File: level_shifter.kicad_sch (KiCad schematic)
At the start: 13 parts, among them U11 74LVC8T245, U12 74AVC4T245, U13 74LVC8T245

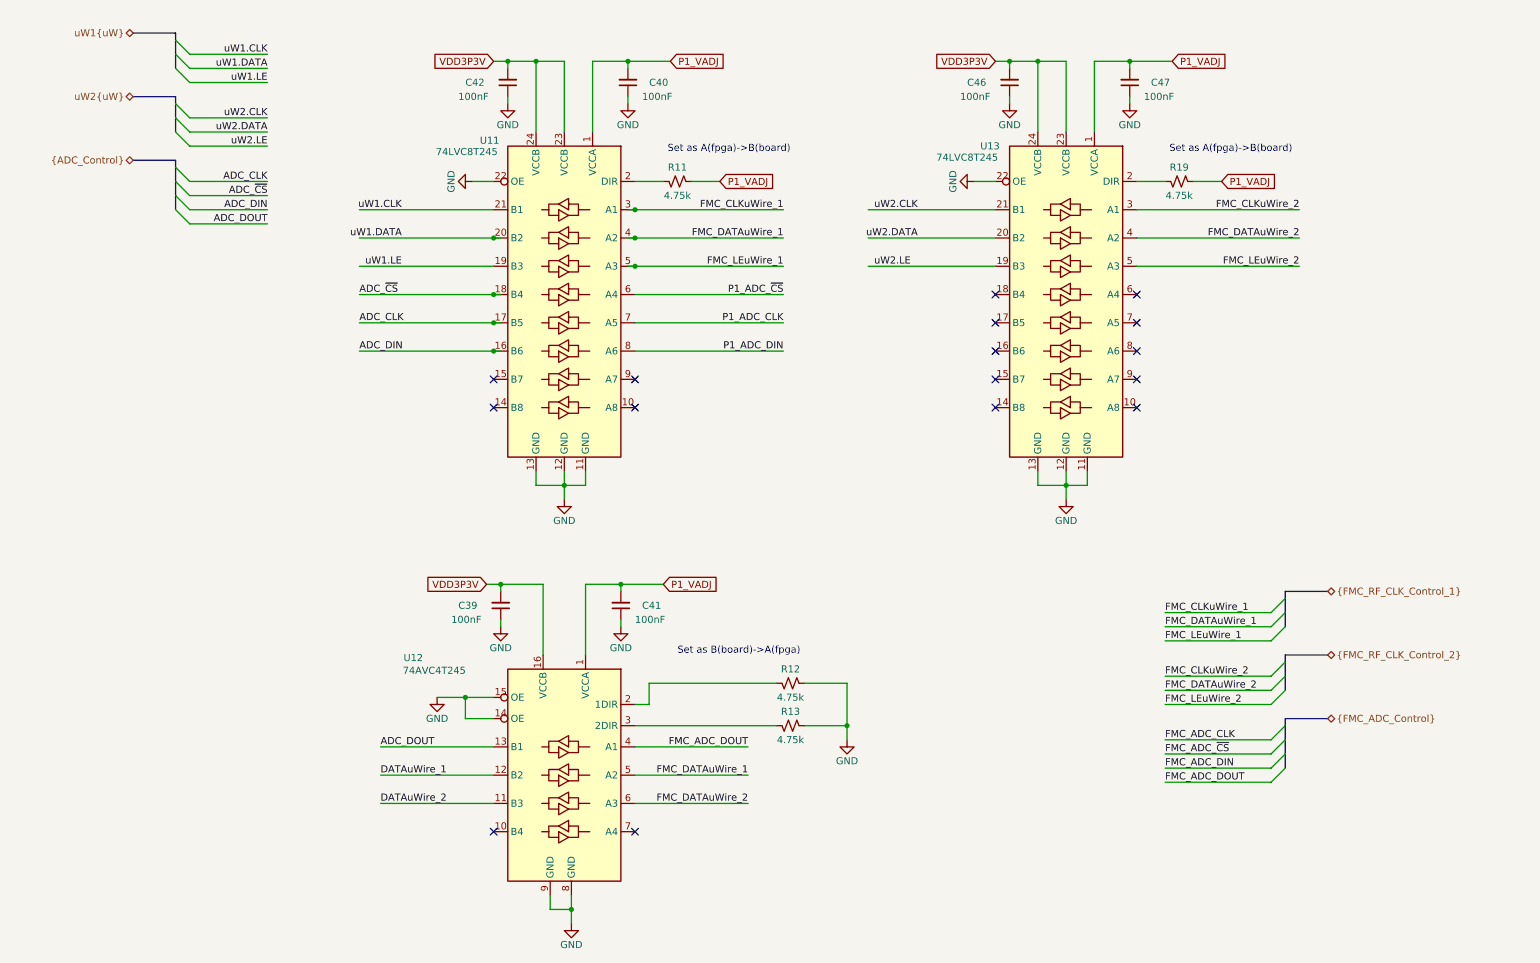
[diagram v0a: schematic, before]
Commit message: Schamtic Revision
- Added 8 more D inputs
- Removed 1 LMK01801 IC
- Cleaned up some buses
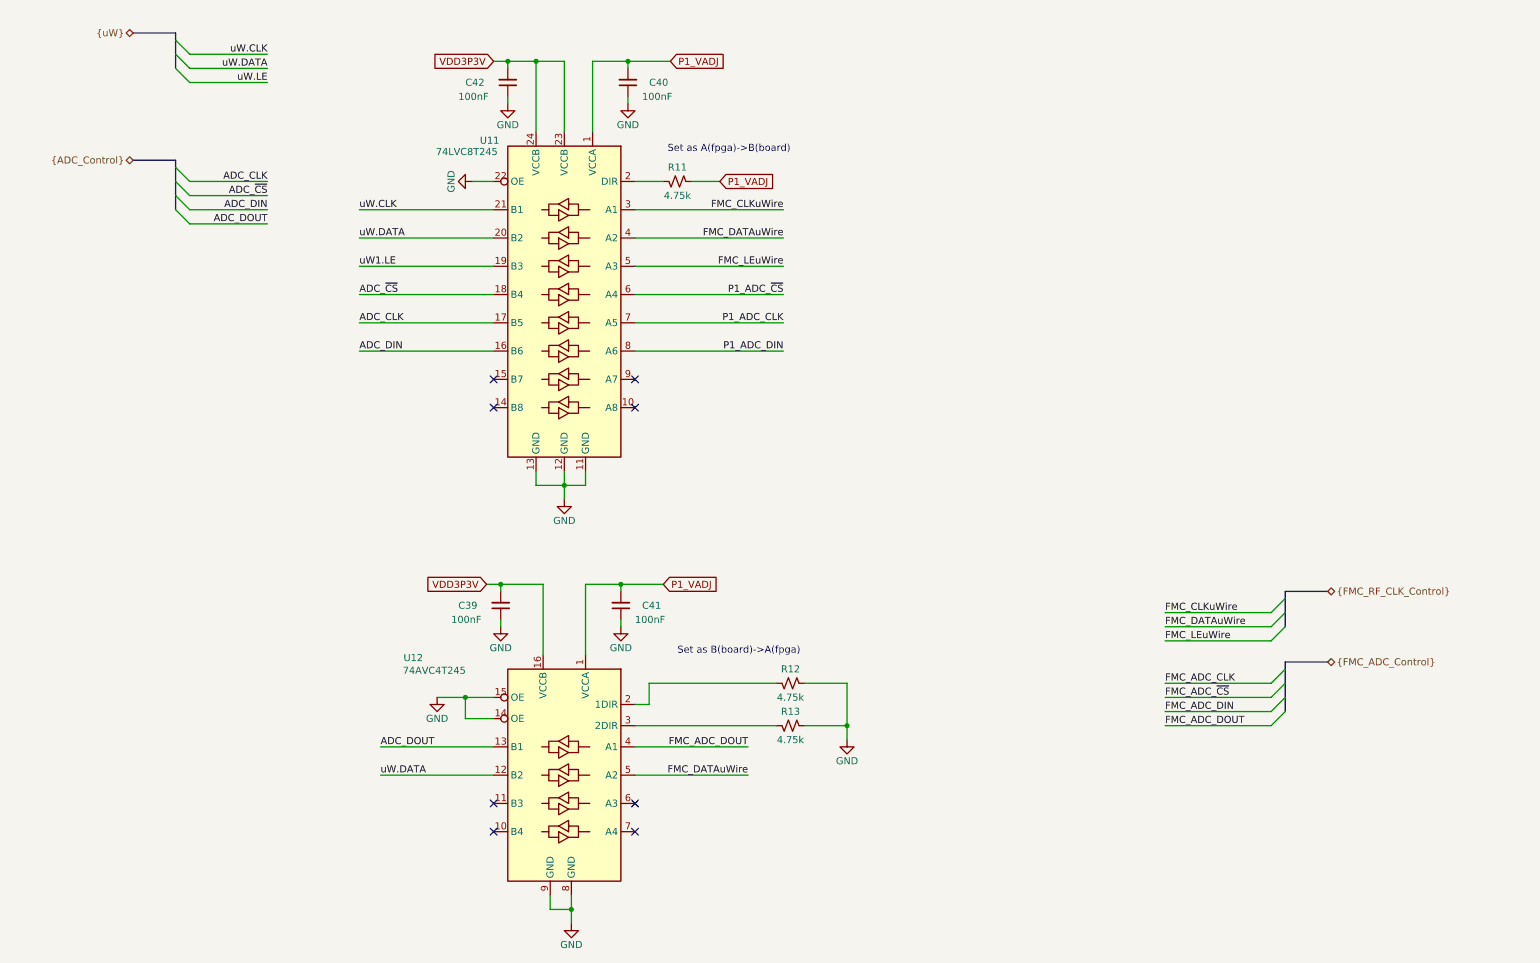
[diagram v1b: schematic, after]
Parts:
- removed C46, C47: 100nF, Capacitor_SMD:C_0402_1005Metric, symbol Device:C_Small
- removed R19: 4.75k, Resistor_SMD:R_0603_1608Metric, symbol Device:R_Small_US
- removed U13: 74LVC8T245, Package_SO:TSSOP-24_4.4x7.8mm_P0.65mm, symbol Custom_Lib_MPEX_Zest:74LVC8T245
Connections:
- net uW1.DATA is gone; now on net uW.DATA: U11.20 (B2)
- net DATAuWire_1 renamed uW.DATA
- net DATAuWire_2: no longer names the net of U12.11 (B3)
- net FMC_CLKuWire_1 renamed FMC_CLKuWire
- net FMC_DATAuWire_1 renamed FMC_DATAuWire
- net FMC_DATAuWire_2: no longer names the net of U12.6 (A3)
- net FMC_LEuWire_1 renamed FMC_LEuWire
- net uW1.CLK renamed uW.CLK
- no-connect marks 16 -> 8

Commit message: Draft Schematic Revision
Schematic should be in good shape.
Meta-data and BOM need to be finished.
Very rough layout was started to floorplan out main parts and to see if we have room.
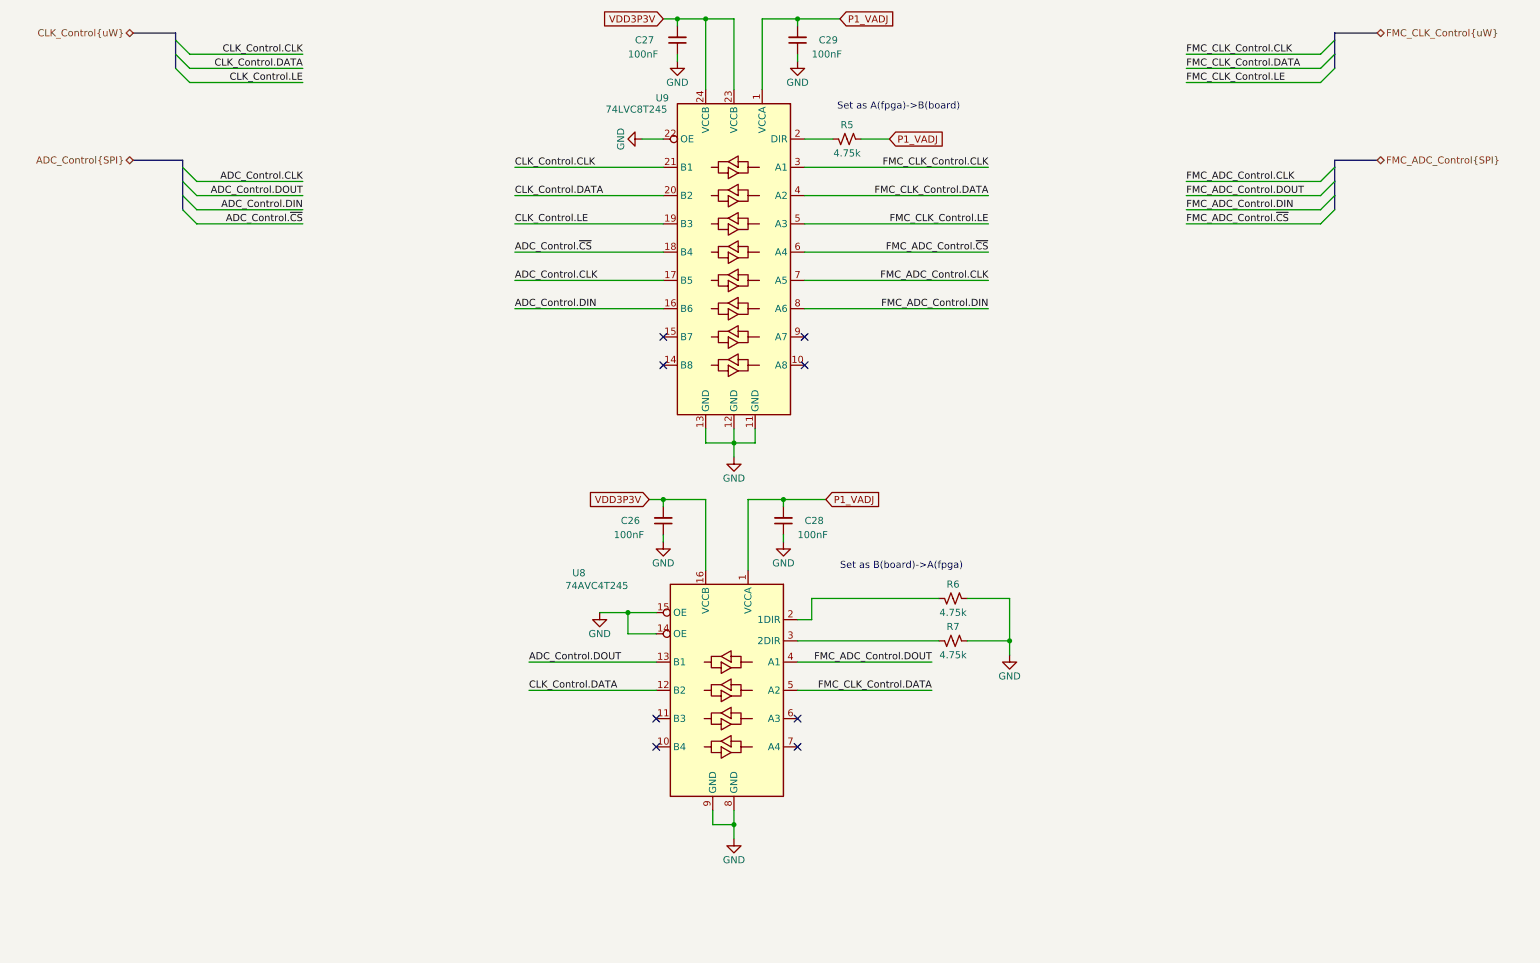
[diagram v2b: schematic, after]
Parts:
- U8: renamed from U12; symbol Custom_Lib_MPEX_Zest:74LVC4T245 -> rf-input-fmc:74LVC4T245
- U9: renamed from U11; symbol Custom_Lib_MPEX_Zest:74LVC8T245 -> rf-input-fmc:74LVC8T245
- renumbered C39 to C26, C42 to C27, C41 to C28, C40 to C29, R11 to R5, R12 to R6, R13 to R7
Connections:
- net ADC_CLK renamed ADC_Control.CLK
- net ADC_DIN renamed ADC_Control.DIN
- net ADC_DOUT renamed ADC_Control.DOUT
- net ADC_~{CS} renamed ADC_Control.~{CS}
- net FMC_ADC_DOUT renamed FMC_ADC_Control.DOUT
- net FMC_CLKuWire renamed FMC_CLK_Control.CLK
- net FMC_DATAuWire renamed FMC_CLK_Control.DATA
- net FMC_LEuWire renamed FMC_CLK_Control.LE
- net P1_ADC_CLK renamed FMC_ADC_Control.CLK
- net P1_ADC_DIN renamed FMC_ADC_Control.DIN
- net P1_ADC_~{CS} renamed FMC_ADC_Control.~{CS}
- net uW.CLK renamed CLK_Control.CLK
- net uW.DATA renamed CLK_Control.DATA
- net uW1.LE renamed CLK_Control.LE
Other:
- moved on the sheet: C26, C27, C28, C29, R5, R6, R7, U8, U9

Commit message: add copyright/license
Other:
- company: Osprey DCS -> SPDX-FileCopyrightText: 2025 Osprey DCS
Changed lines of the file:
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@@
 		(date "2025-10-01")
 		(rev "0.1")
-		(company "Osprey DCS")
-		(comment 1 "Pedro Rodriguez")
+		(company "SPDX-FileCopyrightText: 2025 Osprey DCS")
+		(comment 1 "SPDX-License-Identifier: CERN-OHL-S-2.0+")
 	)
 	(bus_alias "uW"
